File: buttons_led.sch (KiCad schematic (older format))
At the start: 24 parts, among them Q1301 2N7002P, SW1301 SW_Push, SW1302 SW_Push, SW1303 SW_Push, SW1304 SW_Push, SW1305 SW_Push, SW1306 SW_Push

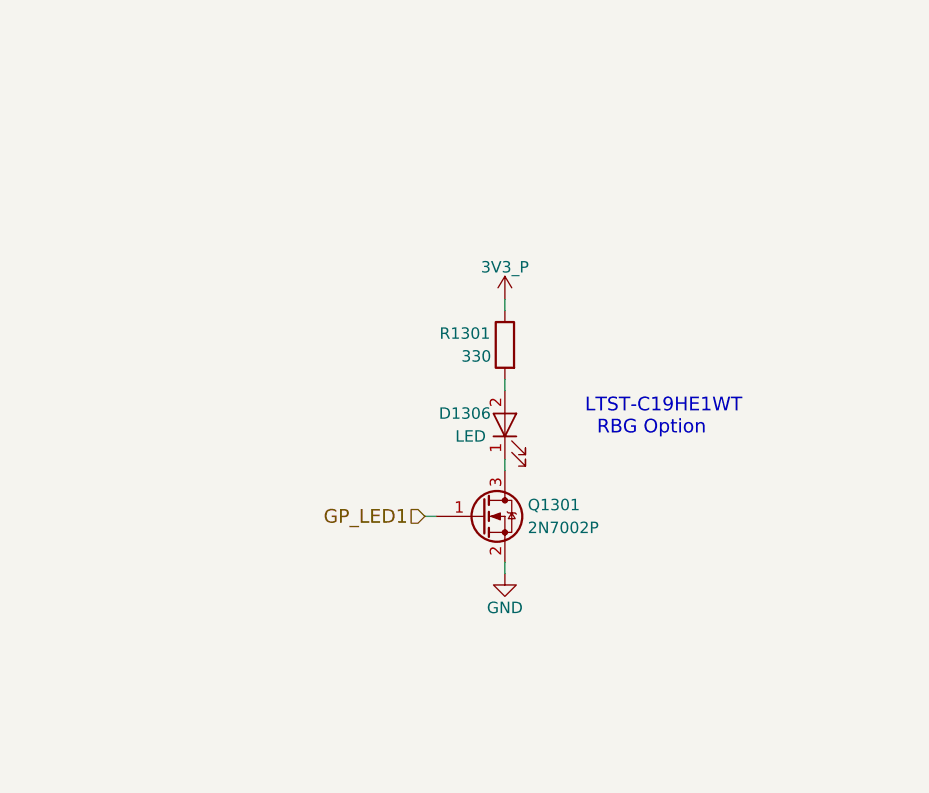
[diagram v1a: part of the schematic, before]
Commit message: Add NOR flash chip schematic, use mini-HDMI (requested) instead of micro and add its corresponding properties and footprint, use 3.5mm CTIA headset jack with through-hole pins rather than an SMD one for extra "mechanical rigidity"
Will likely want to use a USB-C receptacle with through-hole shield pins.
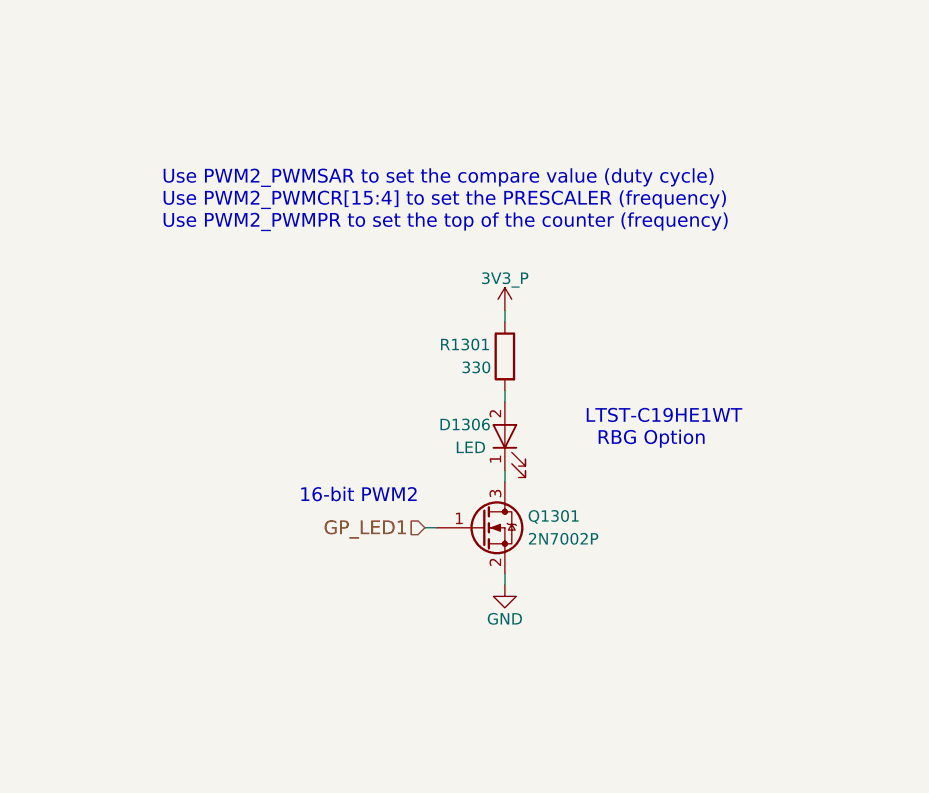
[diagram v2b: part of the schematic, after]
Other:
- note added: "16-bit PWM2"
- note added: "Use PWM2_PWMSAR to set the compare value (duty cycle)\nUse PWM2_PWMCR[15:4] to set the PRESCALER (frequency)\nUse PWM2_PWMPR to set the top of the counter (frequency)"
- moved on the sheet: D1306, Q1301, R1301
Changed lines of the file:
@@
 $Descr A4 11693 8268
 encoding utf-8
-Sheet 12 19
+Sheet 12 20
 Title "Buttons & LED"
-Date "2018-05-02"
+Date "2018-05-14"
 Rev "v0.1.0"
 Comp "Purism SPC"
@@
 L LED D1306
 U 1 1 5ACC7C6F
-P 8750 3300
-F 0 "D1306" V 8800 3475 50  0000 C CNN
-F 1 "LED" V 8700 3450 50  0000 C CNN
-F 2 "" H 8750 3300 50  0001 C CNN
-F 3 "" H 8750 3300 50  0001 C CNN
-	1    8750 3300
+P 8750 3350
+F 0 "D1306" V 8800 3525 50  0000 C CNN
+F 1 "LED" V 8700 3500 50  0000 C CNN
+F 2 "" H 8750 3350 50  0001 C CNN
+F 3 "" H 8750 3350 50  0001 C CNN
+	1    8750 3350
 	0    -1   -1   0
 $EndComp
@@
 L Q_NMOS_GSD Q1301
 U 1 1 5ACC7CF3
-P 8650 3700
-F 0 "Q1301" H 8850 3750 50  0000 L CNN
-F 1 "2N7002P" H 8850 3650 50  0000 L CNN
-F 2 "" H 8850 3800 50  0001 C CNN
-F 3 "" H 8650 3700 50  0001 C CNN
-	1    8650 3700
+P 8650 3750
+F 0 "Q1301" H 8850 3800 50  0000 L CNN
+F 1 "2N7002P" H 8850 3700 50  0000 L CNN
+F 2 "" H 8850 3850 50  0001 C CNN
+F 3 "" H 8650 3750 50  0001 C CNN
+	1    8650 3750
 	1    0    0    -1
 $EndComp
@@
 L GND #PWR0183
 U 1 1 5ACC7D2C
-P 8750 3950
-F 0 "#PWR0183" H 8750 3700 50  0001 C CNN
-F 1 "GND" H 8750 3800 50  0000 C CNN
-F 2 "" H 8750 3950 50  0001 C CNN
-F 3 "" H 8750 3950 50  0001 C CNN
-	1    8750 3950
+P 8750 4000
+F 0 "#PWR0183" H 8750 3750 50  0001 C CNN
+F 1 "GND" H 8750 3850 50  0000 C CNN
+F 2 "" H 8750 4000 50  0001 C CNN
+F 3 "" H 8750 4000 50  0001 C CNN
+	1    8750 4000
 	1    0    0    -1
 $EndComp
@@
 L R R1301
 U 1 1 5ACC7E2E
-P 8750 2950
-F 0 "R1301" H 8925 3000 50  0000 C CNN
-F 1 "330" H 8875 2900 50  0000 C CNN
-F 2 "" V 8680 2950 50  0001 C CNN
-F 3 "" H 8750 2950 50  0001 C CNN
-	1    8750 2950
+P 8750 3000
+F 0 "R1301" H 8925 3050 50  0000 C CNN
+F 1 "330" H 8875 2950 50  0000 C CNN
+F 2 "" V 8680 3000 50  0001 C CNN
+F 3 "" H 8750 3000 50  0001 C CNN
+	1    8750 3000
 	-1   0    0    -1
 $EndComp
 Wire Wire Line
-	8750 2800 8750 2750
-Wire Wire Line
-	8750 3150 8750 3100
-Wire Wire Line
-	8750 3500 8750 3450
-Wire Wire Line
-	8750 3950 8750 3900
-Wire Wire Line
-	8450 3700 8400 3700
+	8750 2850 8750 2800
+Wire Wire Line
+	8750 3200 8750 3150
+Wire Wire Line
+	8750 3550 8750 3500
+Wire Wire Line
+	8750 4000 8750 3950
+Wire Wire Line
+	8450 3750 8400 3750
 Text Label 3700 1300 0    60   ~ 0
 BOOT_CFG04
@@
 Text HLabel 4300 5400 2    60   Output ~ 0
 ONOFF
-Text HLabel 8400 3700 0    60   Input ~ 0
+Text HLabel 8400 3750 0    60   Input ~ 0
 GP_LED1
-Text Notes 9100 3350 0    60   ~ 0
+Text Notes 9100 3400 0    60   ~ 0
 LTST-C19HE1WT\n  RBG Option
 $Comp
 L 3V3_P #PWR0184
 U 1 1 5AEA32FD
-P 8750 2750
-F 0 "#PWR0184" H 8750 2600 50  0001 C CNN
-F 1 "3V3_P" H 8750 2890 50  0000 C CNN
-F 2 "" H 8750 2750 50  0001 C CNN
-F 3 "" H 8750 2750 50  0001 C CNN
-	1    8750 2750
+P 8750 2800
+F 0 "#PWR0184" H 8750 2650 50  0001 C CNN
+F 1 "3V3_P" H 8750 2940 50  0000 C CNN
+F 2 "" H 8750 2800 50  0001 C CNN
+F 3 "" H 8750 2800 50  0001 C CNN
+	1    8750 2800
 	1    0    0    -1
 $EndComp
@@
 Wire Wire Line
 	3650 6550 3650 6650
+Text Notes 7850 3650 0    60   ~ 0
+16-bit PWM2
+Text Notes 7250 2450 0    60   ~ 0
+Use PWM2_PWMSAR to set the compare value (duty cycle)\nUse PWM2_PWMCR[15:4] to set the PRESCALER (frequency)\nUse PWM2_PWMPR to set the top of the counter (frequency)
 $EndSCHEMATC

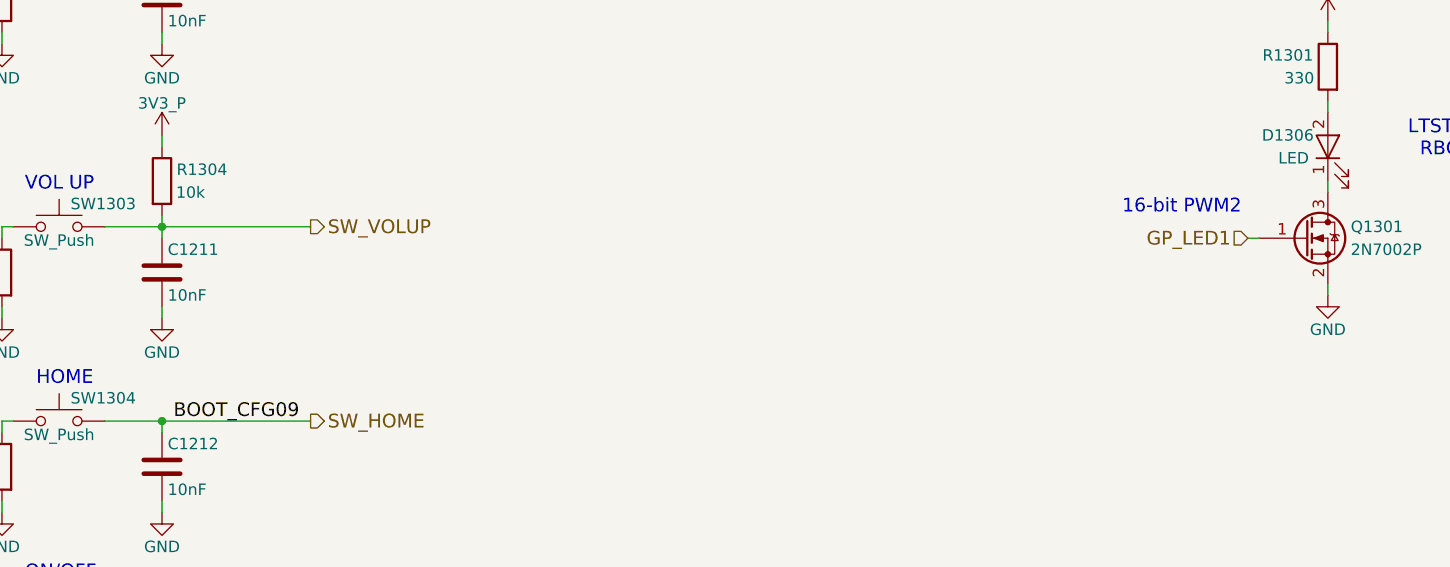
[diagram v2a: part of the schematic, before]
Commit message: Add haptic/vibration motor circuit
Using a PFET to switch the high-side. The motor will likely be coin-shaped with adhesive on the back to stick to a designated spot on the board and have a 2-pin Molex or JST connector installed on the wire leads (by request).
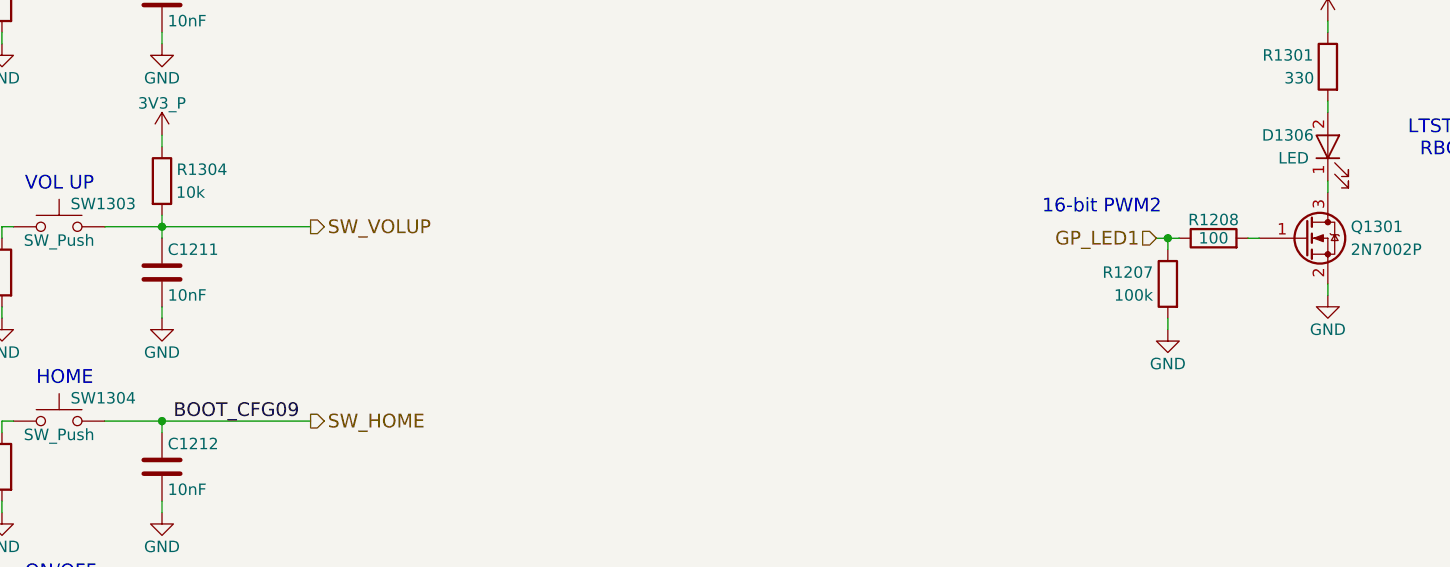
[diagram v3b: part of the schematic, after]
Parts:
- added R1207: 100k, symbol R
- added R1208: 100, symbol R
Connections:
- net GND: now also R1207.2
- net GP_LED1: now also R1207.1, R1208.1; no longer Q1301.1 (G)
- new net: Q1301.1 (G), R1208.2
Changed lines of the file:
@@
 $Descr A4 11693 8268
 encoding utf-8
-Sheet 12 20
+Sheet 12 21
 Title "Buttons & LED"
-Date "2018-05-14"
+Date "2018-05-15"
 Rev "v0.1.0"
 Comp "Purism SPC"
@@
 Wire Wire Line
 	8750 4000 8750 3950
-Wire Wire Line
-	8450 3750 8400 3750
 Text Label 3700 1300 0    60   ~ 0
 BOOT_CFG04
@@
 Text HLabel 4300 5400 2    60   Output ~ 0
 ONOFF
-Text HLabel 8400 3750 0    60   Input ~ 0
+Text HLabel 8000 3750 0    60   Input ~ 0
 GP_LED1
 Text Notes 9100 3400 0    60   ~ 0
@@
 	3400 3700 4300 3700
 Wire Wire Line
-	3650 3750 3650 3650
+	3650 3650 3650 3750
 $Comp
 L C C1212
@@
 Wire Wire Line
 	3650 6550 3650 6650
-Text Notes 7850 3650 0    60   ~ 0
+Text Notes 7500 3650 0    60   ~ 0
 16-bit PWM2
 Text Notes 7250 2450 0    60   ~ 0
 Use PWM2_PWMSAR to set the compare value (duty cycle)\nUse PWM2_PWMCR[15:4] to set the PRESCALER (frequency)\nUse PWM2_PWMPR to set the top of the counter (frequency)
+$Comp
+L R R1207
+U 1 1 5AFF5FC7
+P 8050 3950
+F 0 "R1207" H 8225 4000 50  0000 C CNN
+F 1 "100k" H 8200 3900 50  0000 C CNN
+F 2 "" V 7980 3950 50  0001 C CNN
+F 3 "" H 8050 3950 50  0001 C CNN
+	1    8050 3950
+	-1   0    0    -1
+$EndComp
+$Comp
+L R R1208
+U 1 1 5AFF6F1F
+P 8250 3750
+F 0 "R1208" V 8330 3750 50  0000 C CNN
+F 1 "100" V 8250 3750 50  0000 C CNN
+F 2 "" V 8180 3750 50  0001 C CNN
+F 3 "" H 8250 3750 50  0001 C CNN
+	1    8250 3750
+	0    -1   -1   0
+$EndComp
+Wire Wire Line
+	8000 3750 8100 3750
+Wire Wire Line
+	8400 3750 8450 3750
+Wire Wire Line
+	8050 3800 8050 3750
+Connection ~ 8050 3750
+$Comp
+L GND #PWR0195
+U 1 1 5AFF8032
+P 8050 4150
+F 0 "#PWR0195" H 8050 3900 50  0001 C CNN
+F 1 "GND" H 8050 4000 50  0000 C CNN
+F 2 "" H 8050 4150 50  0001 C CNN
+F 3 "" H 8050 4150 50  0001 C CNN
+	1    8050 4150
+	1    0    0    -1
+$EndComp
+Wire Wire Line
+	8050 4150 8050 4100
 $EndSCHEMATC
